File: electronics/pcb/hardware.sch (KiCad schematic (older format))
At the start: 36 parts, among them U2 A33

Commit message: Schematic review.
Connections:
- net ram/!CAS: now also U2.M3 (DCAS); no longer U2.L4 (DRAS)
- net ram/!RAS: now also U2.L4 (DRAS); no longer U2.M3 (DCAS)
- net ram/!UDQS: now also U2.T1 (DQS1B); no longer U2.R1 (DQS1)
- net ram/UDQS: now also U2.R1 (DQS1); no longer U2.T1 (DQS1B)
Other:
- moved on the sheet: C59
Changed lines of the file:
@@
 F6 "CK" I L 2650 5800 50
 F7 "!CK" I L 2650 5700 50
-F8 "!RAS" I L 2650 6200 50
-F9 "!CAS" I L 2650 6100 50
+F8 "!RAS" I L 2650 6100 50
+F9 "!CAS" I L 2650 6200 50
 F10 "ODT" I L 2650 5900 50
 F11 "!LDQS" I R 3550 5500 50
-F12 "!UDQS" I R 3550 5900 50
+F12 "!UDQS" I R 3550 5800 50
 F13 "LDQS" I R 3550 5600 50
-F14 "UDQS" I R 3550 5800 50
+F14 "UDQS" I R 3550 5900 50
 F15 "LDM" I R 3550 5400 50
 F16 "UDM" I R 3550 5700 50
@@
 L Device:C_Small C?
 U 1 1 60AEEC69
-P 6500 3750
+P 6650 3750
 AR Path="/60536DA4/60AEEC69" Ref="C?"  Part="1"
 AR Path="/60AEEC69" Ref="C59"  Part="1"
-F 0 "C59" V 6550 3800 50  0000 L CNN
-F 1 "100nF" V 6450 3800 50  0000 L CNN
-F 2 "Capacitor_SMD:C_0402_1005Metric" H 6500 3750 50  0001 C CNN
-F 3 "~" H 6500 3750 50  0001 C CNN
-	1    6500 3750
-	1    0    0    -1
-$EndComp
-Wire Wire Line
-	6500 3650 6500 3400
+F 0 "C59" V 6700 3800 50  0000 L CNN
+F 1 "100nF" V 6600 3800 50  0000 L CNN
+F 2 "Capacitor_SMD:C_0402_1005Metric" H 6650 3750 50  0001 C CNN
+F 3 "~" H 6650 3750 50  0001 C CNN
+	1    6650 3750
+	1    0    0    -1
+$EndComp
+Wire Wire Line
+	6650 3650 6650 3400
 Wire Wire Line
 	6900 3400 6900 3350
@@
 	6900 3650 6900 3400
 Wire Wire Line
-	6500 3850 6500 3950
+	6650 3850 6650 3950
 Wire Wire Line
 	7300 3850 7300 3950
@@
 	5300 5000 5500 5000
 Wire Wire Line
-	6500 3400 6900 3400
-Wire Wire Line
-	6500 3950 6900 3950
+	6650 3400 6900 3400
+Wire Wire Line
+	6650 3950 6900 3950
 $Comp
 L Mechanical:MountingHole H2

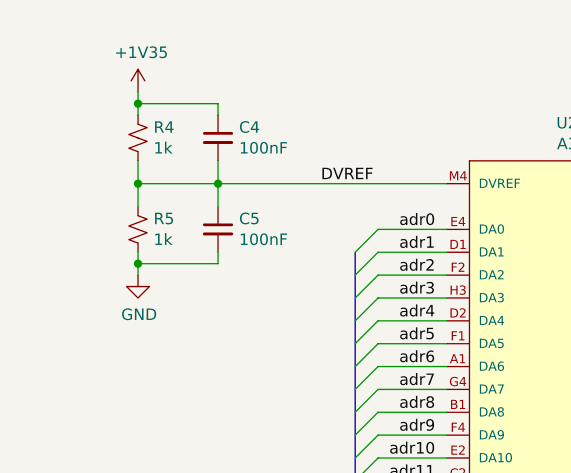
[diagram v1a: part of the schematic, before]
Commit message: Added tolerances
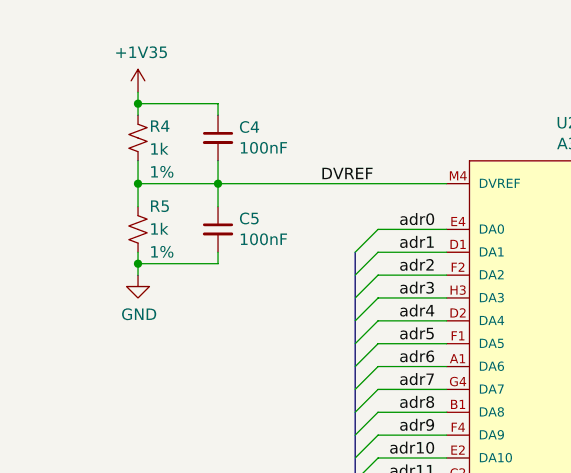
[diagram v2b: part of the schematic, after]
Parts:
- R4, R5: Tolerance (none) -> 1%
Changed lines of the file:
@@
 AR Path="/60536DA4/607B18B2" Ref="R?"  Part="1"
 AR Path="/607B18B2" Ref="R4"  Part="1"
-F 0 "R4" H 1268 1446 50  0000 L CNN
-F 1 "1k" H 1268 1355 50  0000 L CNN
+F 0 "R4" H 1250 1450 50  0000 L CNN
+F 1 "1k" H 1250 1350 50  0000 L CNN
 F 2 "Resistor_SMD:R_0402_1005Metric" H 1200 1400 50  0001 C CNN
 F 3 "~" H 1200 1400 50  0001 C CNN
+F 4 "1%" H 1250 1250 50  0000 L CNN "Tolerance"
 	1    1200 1400
 	1    0    0    -1
@@
 AR Path="/60536DA4/607B18B8" Ref="R?"  Part="1"
 AR Path="/607B18B8" Ref="R5"  Part="1"
-F 0 "R5" H 1268 1846 50  0000 L CNN
-F 1 "1k" H 1268 1755 50  0000 L CNN
+F 0 "R5" H 1250 1900 50  0000 L CNN
+F 1 "1k" H 1250 1800 50  0000 L CNN
 F 2 "Resistor_SMD:R_0402_1005Metric" H 1200 1800 50  0001 C CNN
 F 3 "~" H 1200 1800 50  0001 C CNN
+F 4 "1%" H 1250 1700 50  0000 L CNN "Tolerance"
 	1    1200 1800
 	1    0    0    -1

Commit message: Working through the checklist
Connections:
- net +3V0: no longer U2.M11 (VCC-PD), U2.N11 (VCC-PD)
- net +3V3: now also U2.M11 (VCC-PD), U2.N11 (VCC-PD)
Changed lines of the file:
@@
 	8600 3000 7800 3000
-Wire Wire Line
-	7800 3000 7800 2900
-Wire Wire Line
-	8600 2900 7800 2900
-Connection ~ 7800 2900
-Wire Wire Line
-	7800 2900 7800 2800
-Wire Wire Line
-	8600 2800 7800 2800
-Connection ~ 7800 2800
-Wire Wire Line
-	7800 2800 7800 2700
 Wire Wire Line
 	8600 3300 8450 3300
@@
 F1 "gpio.sch" 50
 $EndSheet
+Text Label 8100 2800 0    50   ~ 0
+VCC-PD
+Wire Wire Line
+	7800 2700 7800 3000
+Wire Wire Line
+	8100 2800 8500 2800
+Wire Wire Line
+	8600 2900 8500 2900
+Wire Wire Line
+	8500 2900 8500 2800
 Wire Bus Line
 	3950 3400 3950 3600
@@
 Wire Bus Line
 	4050 1700 4050 3300
+Connection ~ 8500 2800
+Wire Wire Line
+	8500 2800 8600 2800
+Text Label 7250 4450 0    50   ~ 0
+VCC-PD
 $EndSCHEMATC

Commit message: Removed all the extra fields
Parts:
- U2: DC Supply Voltage for I/O 1.8V ~ 3.3V -> (none); category IC -> (none); ipc land pattern name BGA289N80P17X17_1400X1400X129 -> (none); lead free yes -> (none); library id f6b937119e25c27a -> (none); manufacturer Allwinner Technology Co., Ltd. -> (none); package TFBGA282 -> (none); rohs yes -> (none); temperature range high +125°C -> (none); temperature range low -40°C -> (none)
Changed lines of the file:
@@
 F 2 "A33_FP:Allwinner_Technology_Co.,_Ltd.-A33-0" H 2450 2000 50  0001 L CNN
 F 3 "http://dl.linux-sunxi.org/A33/A33_Datasheet_release1.0.pdf" H 2450 2100 50  0001 L CNN
-F 4 "1.8V ~ 3.3V" H 2450 2200 50  0001 L CNN "DC Supply Voltage for I/O"
-F 5 "IC" H 2450 2300 50  0001 L CNN "category"
-F 6 "BGA289N80P17X17_1400X1400X129" H 2450 2400 50  0001 L CNN "ipc land pattern name"
-F 7 "yes" H 2450 2500 50  0001 L CNN "lead free"
-F 8 "f6b937119e25c27a" H 2450 2600 50  0001 L CNN "library id"
-F 9 "Allwinner Technology Co., Ltd." H 2450 2700 50  0001 L CNN "manufacturer"
-F 10 "TFBGA282" H 2450 2800 50  0001 L CNN "package"
-F 11 "yes" H 2450 2900 50  0001 L CNN "rohs"
-F 12 "+125°C" H 2450 3000 50  0001 L CNN "temperature range high"
-F 13 "-40°C" H 2450 3100 50  0001 L CNN "temperature range low"
-F 14 "" H 2450 3200 50  0001 L CNN "voltage"
 	1    2450 1600
 	1    0    0    -1
@@
 F 2 "A33_FP:Allwinner_Technology_Co.,_Ltd.-A33-0" H 8500 1700 50  0001 L CNN
 F 3 "http://dl.linux-sunxi.org/A33/A33_Datasheet_release1.0.pdf" H 8500 1800 50  0001 L CNN
-F 4 "1.8V ~ 3.3V" H 8500 1900 50  0001 L CNN "DC Supply Voltage for I/O"
-F 5 "IC" H 8500 2000 50  0001 L CNN "category"
-F 6 "BGA289N80P17X17_1400X1400X129" H 8500 2100 50  0001 L CNN "ipc land pattern name"
-F 7 "yes" H 8500 2200 50  0001 L CNN "lead free"
-F 8 "f6b937119e25c27a" H 8500 2300 50  0001 L CNN "library id"
-F 9 "Allwinner Technology Co., Ltd." H 8500 2400 50  0001 L CNN "manufacturer"
-F 10 "TFBGA282" H 8500 2500 50  0001 L CNN "package"
-F 11 "yes" H 8500 2600 50  0001 L CNN "rohs"
-F 12 "+125°C" H 8500 2700 50  0001 L CNN "temperature range high"
-F 13 "-40°C" H 8500 2800 50  0001 L CNN "temperature range low"
-F 14 "" H 8500 2900 50  0001 L CNN "voltage"
 	2    8500 1300
 	1    0    0    -1

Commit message: Added in all the part numbers
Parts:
- C29: MPN (none) -> CL05A106MQ5NUNC
- C30, C31, C33, C37, C38, C4, C40, C42, C43, C48, C5, C59, C64, C65, C66, C67, C68, C73: MPN (none) -> CC0402KRX7R7BB104
- C53, C54, C55, C56, C69, C70: MPN (none) -> GRM155R60J226ME11D
- R26: MPN (none) -> RC0402JR-070RL
- R27, R28: MPN (none) -> RC0402JR-0722RL
- R4, R5: MPN (none) -> 4-1879208-9
- R6: MPN (none) -> 0402WGF2400TCE; Tolerance (none) -> 1%
- U2: MPN (none) -> A33

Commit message: Part numbers are _properly_ in now.
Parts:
- R6: Tolerance 1% -> (none)
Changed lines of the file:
@@
 F 3 "~" H 2450 2100 50 0001 L CNN
 F 4 "A33" H 3100 1965 50 0001 C CNN "MPN"
+F 5 "~" H 3100 1965 50 0001 C CNN "Tolerance"
 	1    2450 1600
 	1    0    0    -1
@@
 F 3 "~" H 1550 1400 50 0001 C CNN
 F 4 "CC0402KRX7R7BB104" H 1642 1546 50 0001 C CNN "MPN"
+F 5 "~" H 1642 1546 50 0001 C CNN "Tolerance"
 	1    1550 1400
 	1    0    0    -1
@@
 F 3 "~" H 1550 1800 50 0001 C CNN
 F 4 "CC0402KRX7R7BB104" H 1642 1946 50 0001 C CNN "MPN"
+F 5 "~" H 1642 1946 50 0001 C CNN "Tolerance"
 	1    1550 1800
 	1    0    0    -1
@@
 F 3 "~" H 2400 4900 50 0001 C CNN
 F 4 "0402WGF2400TCE" H 2350 4900 50 0001 C CNN "MPN"
-F 5 "1%" H 2350 4900 50 0001 C CNN "Tolerance"
+F 5 "~" H 2350 4900 50 0001 C CNN "Tolerance"
 	1    2400 4900
 	0    1    1    0
@@
 F 3 "~" H 8500 1800 50 0001 L CNN
 F 4 "A33" H 9350 1665 50 0001 C CNN "MPN"
+F 5 "~" H 9350 1665 50 0001 C CNN "Tolerance"
 	2    8500 1300
 	1    0    0    -1
@@
 F 3 "~" H 6350 2500 50 0001 C CNN
 F 4 "RC0402JR-070RL" H 6418 2646 50 0001 C CNN "MPN"
+F 5 "~" H 6418 2646 50 0001 C CNN "Tolerance"
 	1    6350 2500
 	0    1    1    0
@@
 F 3 "~" H 6100 1650 50 0001 C CNN
 F 4 "CL05A106MQ5NUNC" H 6100 1850 50 0001 C CNN "MPN"
+F 5 "~" H 6100 1850 50 0001 C CNN "Tolerance"
 	1    6100 1650
 	1    0    0    -1
@@
 F 3 "~" H 6400 1650 50 0001 C CNN
 F 4 "CC0402KRX7R7BB104" H 6400 1850 50 0001 C CNN "MPN"
+F 5 "~" H 6400 1850 50 0001 C CNN "Tolerance"
 	1    6400 1650
 	1    0    0    -1
@@
 F 3 "~" H 4900 1500 50 0001 C CNN
 F 4 "CC0402KRX7R7BB104" H 4950 1650 50 0001 C CNN "MPN"
+F 5 "~" H 4950 1650 50 0001 C CNN "Tolerance"
 	1    4900 1500
 	1    0    0    -1
@@
 F 3 "~" H 5100 1500 50 0001 C CNN
 F 4 "CC0402KRX7R7BB104" H 5150 1650 50 0001 C CNN "MPN"
+F 5 "~" H 5150 1650 50 0001 C CNN "Tolerance"
 	1    5100 1500
 	1    0    0    -1
@@
 F 3 "~" H 5300 1500 50 0001 C CNN
 F 4 "CC0402KRX7R7BB104" H 5350 1650 50 0001 C CNN "MPN"
+F 5 "~" H 5350 1650 50 0001 C CNN "Tolerance"
 	1    5300 1500
 	1    0    0    -1
@@
 F 3 "~" H 5500 1500 50 0001 C CNN
 F 4 "GRM155R60J226ME11D" H 5550 1650 50 0001 C CNN "MPN"
+F 5 "~" H 5550 1650 50 0001 C CNN "Tolerance"
 	1    5500 1500
 	1    0    0    -1
@@
 F 3 "~" H 5000 2700 50 0001 C CNN
 F 4 "CC0402KRX7R7BB104" H 5050 2850 50 0001 C CNN "MPN"
+F 5 "~" H 5050 2850 50 0001 C CNN "Tolerance"
 	1    5000 2700
 	1    0    0    -1
@@
 F 3 "~" H 5200 2700 50 0001 C CNN
 F 4 "CC0402KRX7R7BB104" H 5250 2850 50 0001 C CNN "MPN"
+F 5 "~" H 5250 2850 50 0001 C CNN "Tolerance"
 	1    5200 2700
 	1    0    0    -1
@@
 F 3 "~" H 5400 2700 50 0001 C CNN
 F 4 "GRM155R60J226ME11D" H 5450 2850 50 0001 C CNN "MPN"
+F 5 "~" H 5450 2850 50 0001 C CNN "Tolerance"
 	1    5400 2700
 	1    0    0    -1
@@
 F 3 "~" H 5300 3750 50 0001 C CNN
 F 4 "CC0402KRX7R7BB104" H 5350 3900 50 0001 C CNN "MPN"
+F 5 "~" H 5350 3900 50 0001 C CNN "Tolerance"
 	1    5300 3750
 	1    0    0    -1
@@
 F 3 "~" H 5500 3750 50 0001 C CNN
 F 4 "GRM155R60J226ME11D" H 5550 3900 50 0001 C CNN "MPN"
+F 5 "~" H 5550 3900 50 0001 C CNN "Tolerance"
 	1    5500 3750
 	1    0    0    -1
@@
 F 3 "~" H 6650 3750 50 0001 C CNN
 F 4 "CC0402KRX7R7BB104" H 6700 3900 50 0001 C CNN "MPN"
+F 5 "~" H 6700 3900 50 0001 C CNN "Tolerance"
 	1    6650 3750
 	1    0    0    -1
@@
 F 3 "~" H 6900 3750 50 0001 C CNN
 F 4 "CC0402KRX7R7BB104" H 6950 3900 50 0001 C CNN "MPN"
+F 5 "~" H 6950 3900 50 0001 C CNN "Tolerance"
 	1    6900 3750
 	1    0    0    -1
@@
 F 3 "~" H 7100 3750 50 0001 C CNN
 F 4 "CC0402KRX7R7BB104" H 7150 3900 50 0001 C CNN "MPN"
+F 5 "~" H 7150 3900 50 0001 C CNN "Tolerance"
 	1    7100 3750
 	1    0    0    -1
@@
 F 3 "~" H 7300 3750 50 0001 C CNN
 F 4 "GRM155R60J226ME11D" H 7350 3900 50 0001 C CNN "MPN"
+F 5 "~" H 7350 3900 50 0001 C CNN "Tolerance"
 	1    7300 3750
 	1    0    0    -1
@@
 F 3 "~" H 5300 4800 50 0001 C CNN
 F 4 "CC0402KRX7R7BB104" H 5350 4950 50 0001 C CNN "MPN"
+F 5 "~" H 5350 4950 50 0001 C CNN "Tolerance"
 	1    5300 4800
 	1    0    0    -1
@@
 F 3 "~" H 5500 4800 50 0001 C CNN
 F 4 "CC0402KRX7R7BB104" H 5550 4950 50 0001 C CNN "MPN"
+F 5 "~" H 5550 4950 50 0001 C CNN "Tolerance"
 	1    5500 4800
 	1    0    0    -1
@@
 F 3 "~" H 6750 4800 50 0001 C CNN
 F 4 "CC0402KRX7R7BB104" H 6800 4950 50 0001 C CNN "MPN"
+F 5 "~" H 6800 4950 50 0001 C CNN "Tolerance"
 	1    6750 4800
 	1    0    0    -1
@@
 F 3 "~" H 6950 4800 50 0001 C CNN
 F 4 "CC0402KRX7R7BB104" H 7000 4950 50 0001 C CNN "MPN"
+F 5 "~" H 7000 4950 50 0001 C CNN "Tolerance"
 	1    6950 4800
 	1    0    0    -1
@@
 F 3 "~" H 7150 4800 50 0001 C CNN
 F 4 "CC0402KRX7R7BB104" H 7200 4950 50 0001 C CNN "MPN"
+F 5 "~" H 7200 4950 50 0001 C CNN "Tolerance"
 	1    7150 4800
 	1    0    0    -1
@@
 F 3 "~" H 7350 4800 50 0001 C CNN
 F 4 "GRM155R60J226ME11D" H 7400 4950 50 0001 C CNN "MPN"
+F 5 "~" H 7400 4950 50 0001 C CNN "Tolerance"
 	1    7350 4800
 	1    0    0    -1
@@
 F 3 "~" H 7950 4300 50 0001 C CNN
 F 4 "CC0402KRX7R7BB104" H 8000 4450 50 0001 C CNN "MPN"
+F 5 "~" H 8000 4450 50 0001 C CNN "Tolerance"
 	1    7950 4300
 	1    0    0    -1
@@
 F 3 "~" H 2200 4300 50 0001 C CNN
 F 4 "RC0402JR-0722RL" H 2150 4500 50 0001 C CNN "MPN"
+F 5 "~" H 2150 4500 50 0001 C CNN "Tolerance"
 	1    2200 4300
 	0    1    1    0
@@
 F 3 "~" H 2200 4400 50 0001 C CNN
 F 4 "RC0402JR-0722RL" H 2150 4600 50 0001 C CNN "MPN"
+F 5 "~" H 2150 4600 50 0001 C CNN "Tolerance"
 	1    2200 4400
 	0    1    1    0
@@
 F 3 "~" H 5700 4800 50 0001 C CNN
 F 4 "GRM155R60J226ME11D" H 5750 4950 50 0001 C CNN "MPN"
+F 5 "~" H 5750 4950 50 0001 C CNN "Tolerance"
 	1    5700 4800
 	1    0    0    -1
@@
 F 2 "MountingHole:MountingHole_3.2mm_M3" H 750 7150 50 0001 C CNN
 F 3 "~" H 750 7150 50 0001 C CNN
+F 4 "~" H 850 7296 50 0001 C CNN "Tolerance"
 	1    750  7150
 	1    0    0    -1
@@
 F 2 "MountingHole:MountingHole_3.2mm_M3" H 750 7350 50 0001 C CNN
 F 3 "~" H 750 7350 50 0001 C CNN
+F 4 "~" H 850 7496 50 0001 C CNN "Tolerance"
 	1    750  7350
 	1    0    0    -1
@@
 F 2 "MountingHole:MountingHole_3.2mm_M3" H 750 7550 50 0001 C CNN
 F 3 "~" H 750 7550 50 0001 C CNN
+F 4 "~" H 850 7696 50 0001 C CNN "Tolerance"
 	1    750  7550
 	1    0    0    -1
@@
 F 2 "MountingHole:MountingHole_3.2mm_M3" H 750 6950 50 0001 C CNN
 F 3 "~" H 750 6950 50 0001 C CNN
+F 4 "~" H 850 7096 50 0001 C CNN "Tolerance"
 	1    750  6950
 	1    0    0    -1
